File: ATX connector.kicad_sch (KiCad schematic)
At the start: 14 parts, among them J402 ATX-24, J403 ATX-20

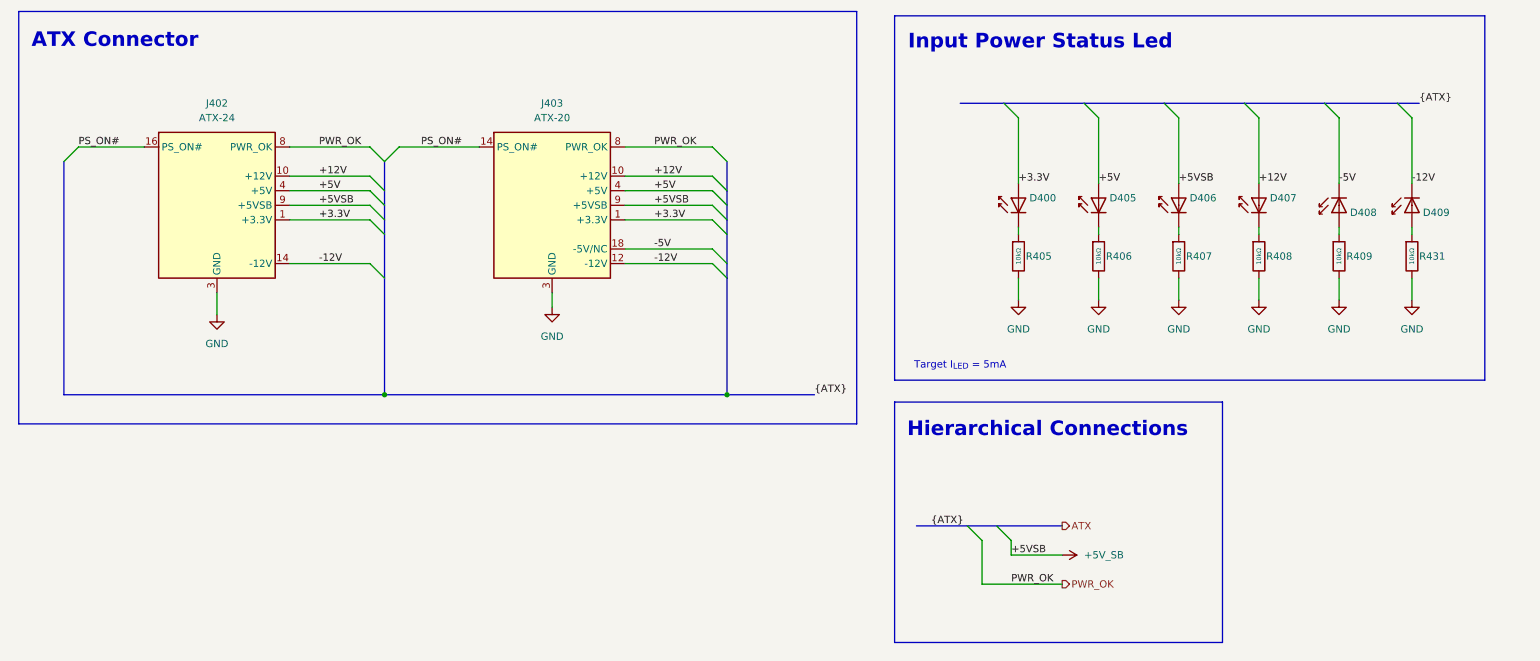
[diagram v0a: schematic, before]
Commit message: added 4 pin ATX connectors
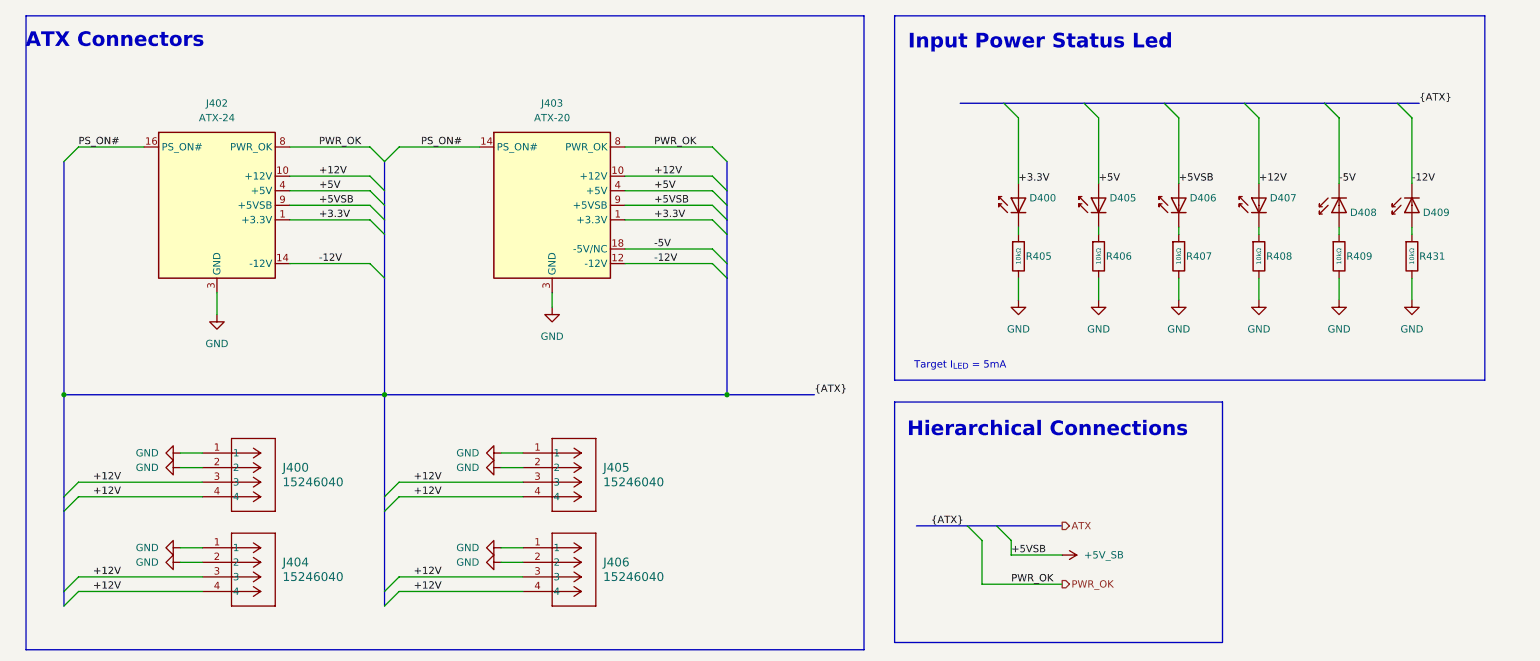
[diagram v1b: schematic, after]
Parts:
- added J400, J404, J405, J406: 15246040, footprints:CONN_SDA-42404_04_MOL, symbol 2025-11-30_18-16-43:15246040
- J403: footprint (none) -> Connector_Molex:Molex_Mini-Fit_Jr_5566-20A2_2x10_P4.20mm_Vertical
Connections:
- net +12V: now also J400.3, J400.4, J404.3, J404.4, J405.3, J405.4, J406.3, J406.4
- net GND: now also J400.1, J400.2, J404.1, J404.2, J405.1, J405.2, J406.1, J406.2
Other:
- note added: "ATX Connectors"
- note removed: "ATX Connector"

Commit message: removed 20pin ATX connector
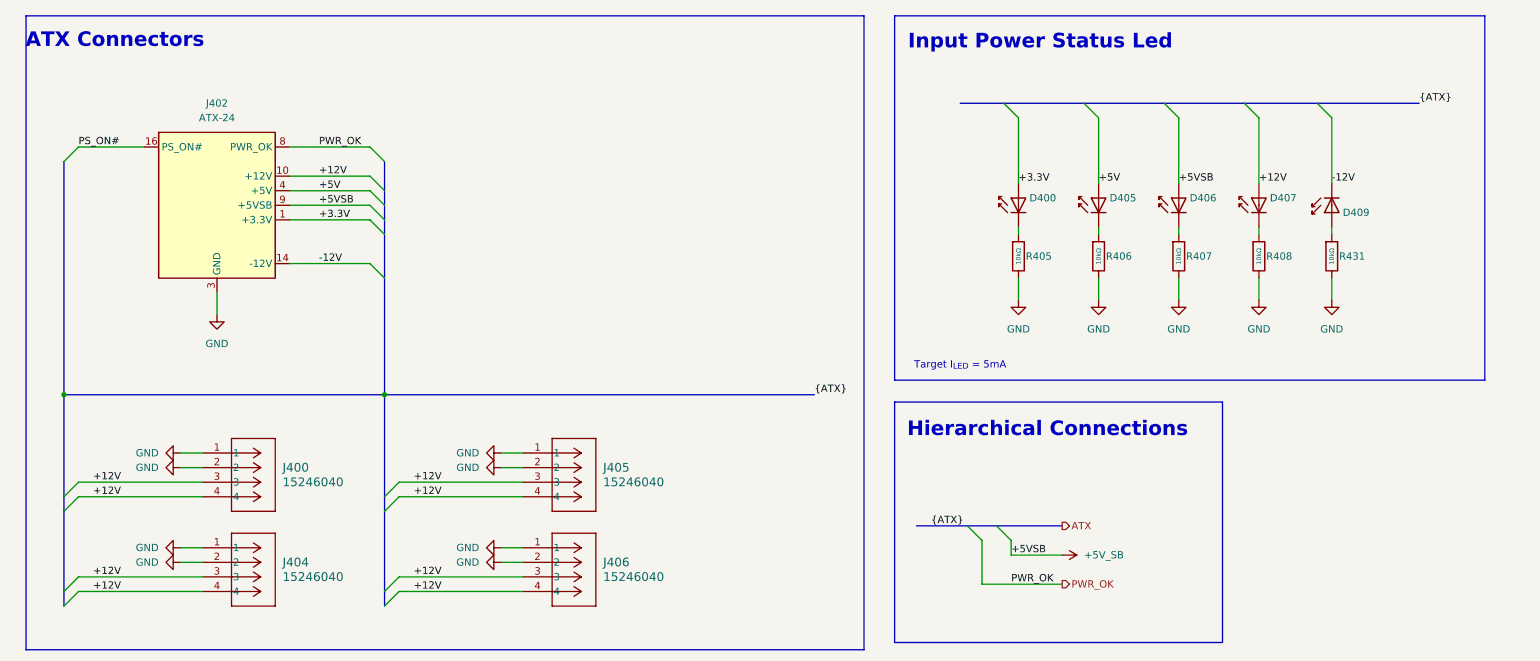
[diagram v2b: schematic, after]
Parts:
- removed D408: Green, PCM_JLCPCB:D_0603, symbol PCM_JLCPCB-Diodes:LED,0603,Green
- removed J403: ATX-20, Connector_Molex:Molex_Mini-Fit_Jr_5566-20A2_2x10_P4.20mm_Vertical, symbol Connector:ATX-20
- removed R409: 10kΩ, PCM_JLCPCB:R_0402, symbol PCM_JLCPCB-Resistors:0402,10kΩ
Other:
- moved on the sheet: D409, R431

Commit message: fixed PS_ON# switching
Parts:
- J402: footprint Connector_Molex:Molex_Mini-Fit_Jr_5566-24A2_2x12_P4.20mm_Vertical -> Connector_Molex:Molex_Mini-Fit_Jr_5569-24A2_2x12_P4.20mm_Horizontal
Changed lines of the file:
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@@
 			)
 		)
-		(property "Footprint" "Connector_Molex:Molex_Mini-Fit_Jr_5566-24A2_2x12_P4.20mm_Vertical"
+		(property "Footprint" "Connector_Molex:Molex_Mini-Fit_Jr_5569-24A2_2x12_P4.20mm_Horizontal"
 			(at 57.15 55.88 0)
 			(effects

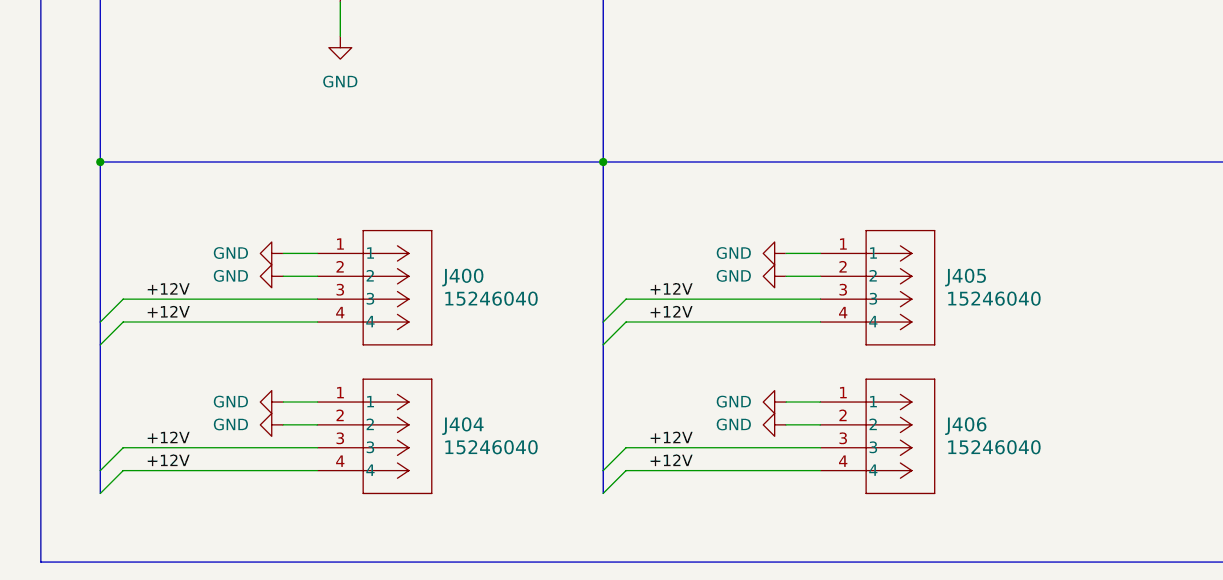
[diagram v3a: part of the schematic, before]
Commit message: removed III out of IV 4 pin connector
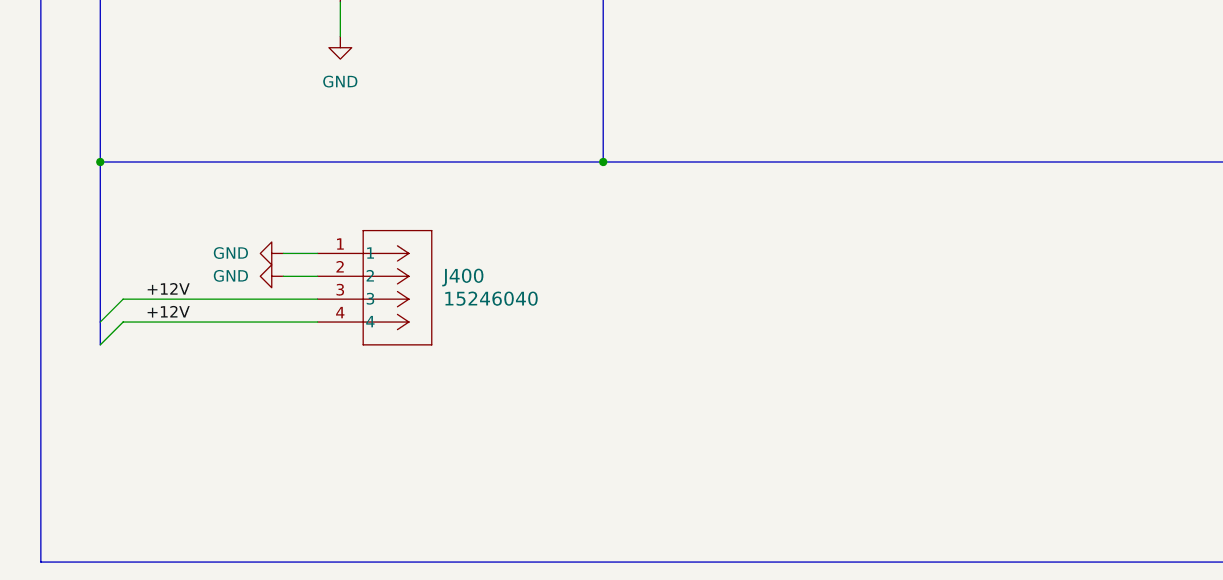
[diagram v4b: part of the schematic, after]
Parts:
- removed J404, J405, J406: 15246040, footprints:CONN_SDA-42404_04_MOL, symbol 2025-11-30_18-16-43:15246040

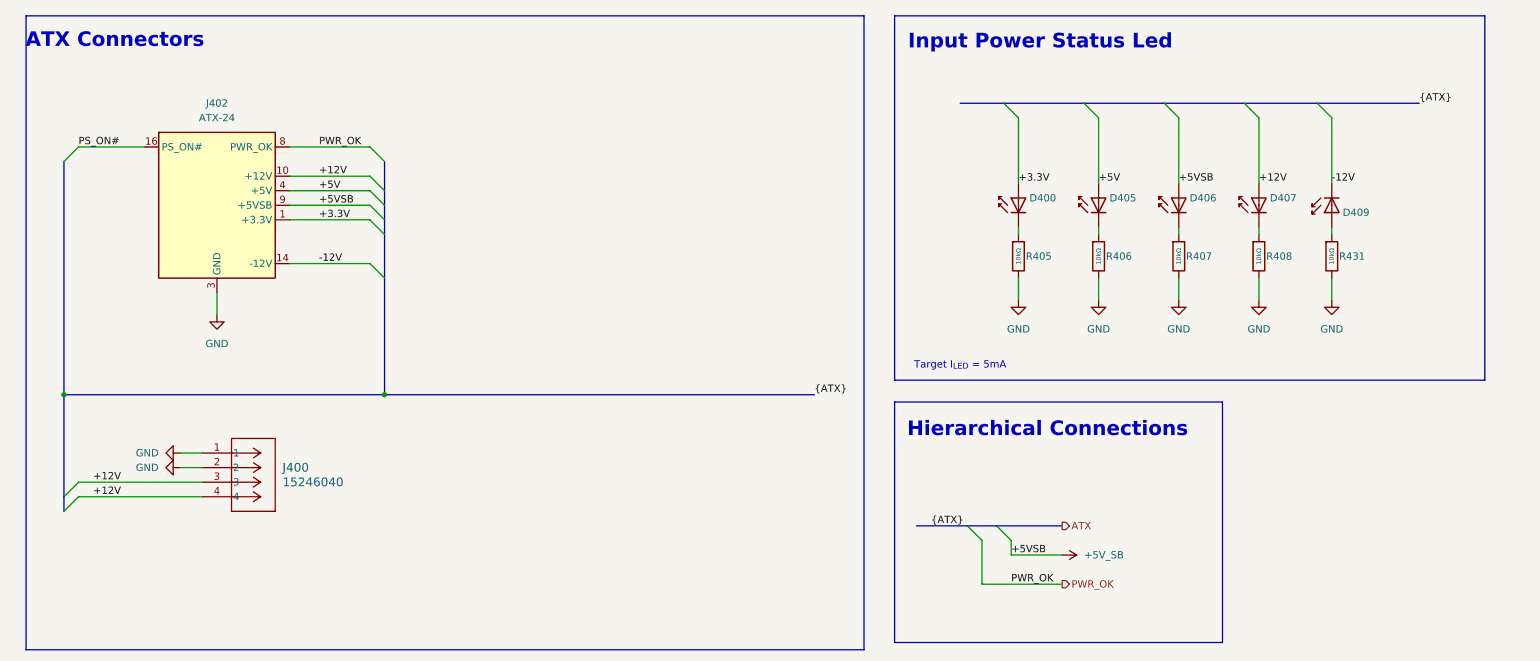
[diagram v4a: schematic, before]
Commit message: removed 3V3 converter
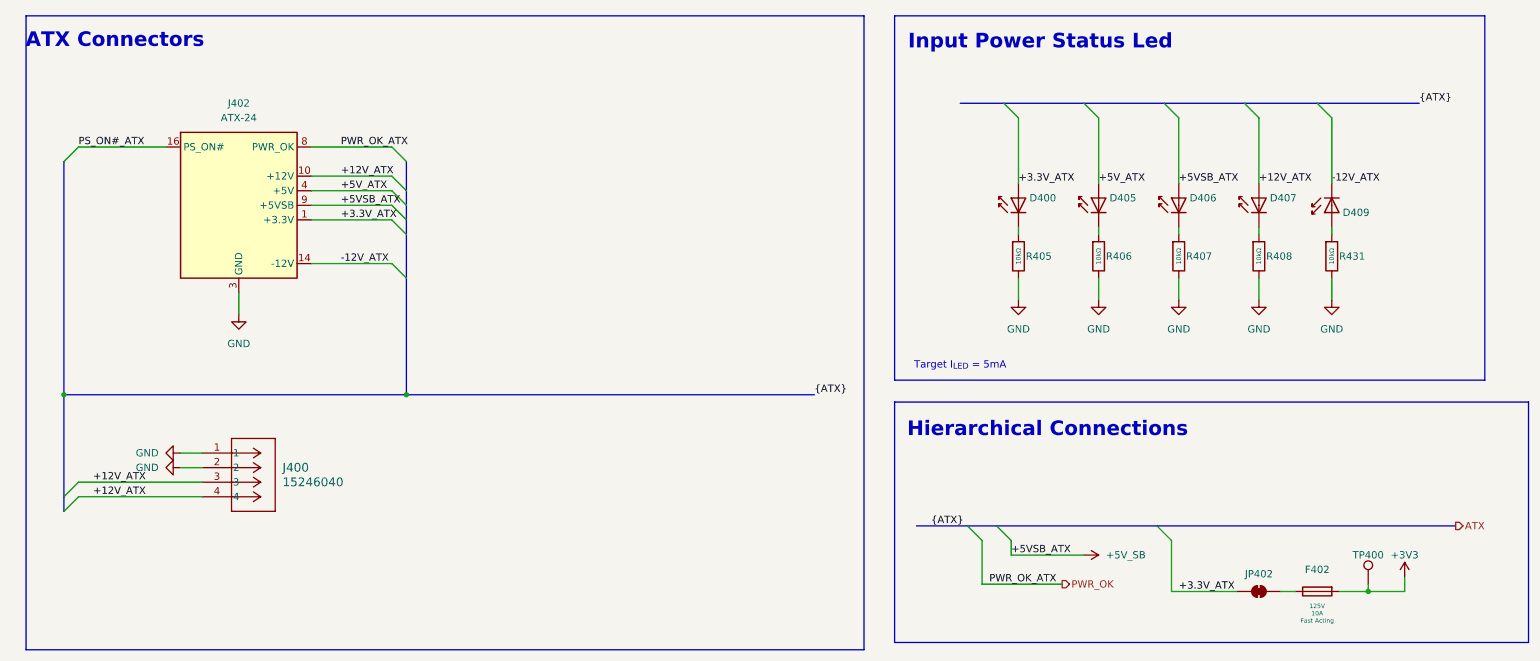
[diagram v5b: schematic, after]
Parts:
- added F402: 10A, FuseCustom:Fuse_2410_6125, symbol FuseCustom:JFC2410FS-2100FS
- added JP402: Test Buck Vout, Jumper:SolderJumper-2_P1.3mm_Open_TrianglePad1.0x1.5mm, symbol Jumper:SolderJumper_2_Bridged
- added TP400: TestPoint, TestPoint:TestPoint_Pad_D1.0mm, symbol Connector:TestPoint
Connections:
- net +12V renamed +12V_ATX
- net +3.3V renamed +3.3V_ATX
- net +3.3V_ATX: now also JP402.1 (A)
- net +5V renamed +5V_ATX
- net -12V renamed -12V_ATX
- net PS_ON# renamed PS_ON#_ATX
- new net: F402.2, JP402.2 (B)
- new net +3V3: F402.1, TP400.1
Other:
- moved on the sheet: J402

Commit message: routing progress
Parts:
- J402: footprint Connector_Molex:Molex_Mini-Fit_Jr_5569-24A2_2x12_P4.20mm_Horizontal -> Connector_Molex:Molex_Mini-Fit_Jr_5566-24A2_2x12_P4.20mm_Vertical
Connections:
- net 3V3_BF: now reaches F402.2, JP402.2 (B)
- net PWR_OK renamed PWR_OK_ATX
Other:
- moved on the sheet: F402, TP400
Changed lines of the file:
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@@
 	)
 	(junction
-		(at 257.81 120.65)
+		(at 269.24 120.65)
 		(diameter 0)
 		(color 0 0 0 0)
@@
 	(wire
 		(pts
-			(xy 252.73 120.65) (xy 257.81 120.65)
+			(xy 264.16 120.65) (xy 269.24 120.65)
 		)
 		(stroke
@@
 	(wire
 		(pts
-			(xy 33.02 43.18) (xy 48.26 43.18)
-		)
-		(stroke
-			(width 0)
-			(type default)
-		)
-	)
-	(wire
-		(pts
 			(xy 54.61 99.06) (xy 50.8 99.06)
 		)
@@
 	(wire
 		(pts
-			(xy 242.57 120.65) (xy 245.11 120.65)
+			(xy 242.57 120.65) (xy 256.54 120.65)
 		)
 		(stroke
@@
 	(wire
 		(pts
-			(xy 257.81 120.65) (xy 264.16 120.65)
+			(xy 269.24 120.65) (xy 275.59 120.65)
 		)
 		(stroke
@@
 	(wire
 		(pts
-			(xy 264.16 118.11) (xy 264.16 120.65)
+			(xy 275.59 118.11) (xy 275.59 120.65)
 		)
 		(stroke
@@
 	(wire
 		(pts
-			(xy 257.81 119.38) (xy 257.81 120.65)
+			(xy 269.24 119.38) (xy 269.24 120.65)
 		)
 		(stroke
@@
 	(wire
 		(pts
+			(xy 33.02 43.18) (xy 48.26 43.18)
+		)
+		(stroke
+			(width 0)
+			(type default)
+		)
+	)
+	(wire
+		(pts
 			(xy 251.46 38.1) (xy 251.46 49.53)
 		)
@@
 		)
 	)
-	(label "{ATX}"
-		(at 181.61 109.22 0)
-		(effects
-			(font
-				(size 1.27 1.27)
-			)
-			(justify left bottom)
-		)
-	)
 	(label "+5V_ATX"
 		(at 78.74 50.8 0)
@@
 	)
 	(label "+5VSB_ATX"
-		(at 78.74 53.34 0)
+		(at 77.47 53.34 0)
 		(effects
 			(font
@@
 		)
 	)
+	(label "{ATX}"
+		(at 181.61 109.22 0)
+		(effects
+			(font
+				(size 1.27 1.27)
+			)
+			(justify left bottom)
+		)
+	)
 	(label "+12V_ATX"
 		(at 35.56 104.14 0)
@@
 	)
 	(label "PS_ON#_ATX"
-		(at 33.02 43.18 0)
+		(at 34.29 43.18 0)
+		(effects
+			(font
+				(size 1.27 1.27)
+			)
+			(justify left bottom)
+		)
+	)
+	(label "3V3_BF"
+		(at 246.38 120.65 0)
 		(effects
 			(font
@@
 		)
 	)
-	(hierarchical_label "PWR_OK"
+	(hierarchical_label "PWR_OK_ATX"
 		(shape output)
 		(at 204.47 119.38 0)
@@
 		)
 	)
-	(hierarchical_label "ATX"
+	(hierarchical_label "ATX{ATX}"
 		(shape output)
 		(at 273.05 109.22 0)
@@
 	(symbol
 		(lib_id "Connector:TestPoint")
-		(at 257.81 119.38 0)
+		(at 269.24 119.38 0)
 		(unit 1)
 		(exclude_from_sim no)
@@
 		(dnp no)
 		(property "Reference" "TP400"
-			(at 257.81 114.3 0)
+			(at 269.24 114.3 0)
 			(effects
 				(font
@@
 		)
 		(property "Value" "TestPoint"
-			(at 260.35 117.348 0)
+			(at 271.78 117.348 0)
 			(effects
 				(font
@@
 		)
 		(property "Footprint" "TestPoint:TestPoint_Pad_D1.0mm"
-			(at 262.89 119.38 0)
+			(at 274.32 119.38 0)
 			(effects
 				(font
@@
 		)
 		(property "Datasheet" "~"
-			(at 262.89 119.38 0)
+			(at 274.32 119.38 0)
 			(effects
 				(font
@@
 		)
 		(property "Description" "test point"
-			(at 257.81 119.38 0)
+			(at 269.24 119.38 0)
 			(effects
 				(font
@@
 	(symbol
 		(lib_id "FuseCustom:JFC2410FS-2100FS")
-		(at 248.92 120.65 270)
+		(at 260.35 120.65 270)
 		(unit 1)
 		(exclude_from_sim no)
@@
 		(dnp no)
 		(property "Reference" "F402"
-			(at 248.92 116.84 90)
+			(at 260.35 116.84 90)
 			(effects
 				(font
@@
 		)
 		(property "Value" "10A"
-			(at 243.84 120.65 0)
+			(at 255.27 120.65 0)
 			(effects
 				(font
@@
 		)
 		(property "Footprint" "FuseCustom:Fuse_2410_6125"
-			(at 244.348 120.65 0)
+			(at 255.778 120.65 0)
 			(effects
 				(font
@@
 		)
 		(property "Datasheet" "https://jlcpcb.com/api/file/downloadByFileSystemAccessId/8588899540782604288"
-			(at 244.094 120.65 0)
+			(at 255.524 120.65 0)
 			(effects
 				(font
@@
 		)
 		(property "Description" "-55℃~+125℃ 10A 125V 125V 50A Surface Mount Fuse 2410 Disposable fuses ROHS"
-			(at 244.094 120.65 0)
+			(at 255.524 120.65 0)
 			(effects
 				(font
@@
 		)
 		(property "Manufacturer" "Shenzhen JDT Fuse"
-			(at 244.348 120.65 0)
+			(at 255.778 120.65 0)
 			(effects
 				(font
@@
 		)
 		(property "Name" "JFC2410FS-2100FS"
-			(at 244.348 120.65 0)
+			(at 255.778 120.65 0)
 			(effects
 				(font
@@
 		)
 		(property "Package" "2410"
-			(at 244.348 120.904 0)
+			(at 255.778 120.904 0)
 			(effects
 				(font
@@
 		)
 		(property "Current Trigger" "10A"
-			(at 248.92 124.46 90)
+			(at 260.35 124.46 90)
 			(do_not_autoplace yes)
 			(effects
@@
 		)
 		(property "Voltage Rating" "125V"
-			(at 248.92 123.19 90)
+			(at 260.35 123.19 90)
 			(do_not_autoplace yes)
 			(effects
@@
 		)
 		(property "Time Sensitivity" "Fast Acting"
-			(at 248.92 125.73 90)
+			(at 260.35 125.73 90)
 			(do_not_autoplace yes)
 			(effects
@@
 		)
 		(property "Assembly Type" "SMT Assembly"
-			(at 244.094 120.396 0)
+			(at 255.524 120.396 0)
 			(effects
 				(font
@@
 		)
 		(property "LCSC" "C136374"
-			(at 244.348 120.65 0)
+			(at 255.778 120.65 0)
 			(effects
 				(font
@@
 	(symbol
 		(lib_id "power:+5V")
-		(at 264.16 118.11 0)
+		(at 275.59 118.11 0)
 		(unit 1)
 		(exclude_from_sim no)
@@
 		(dnp no)
 		(property "Reference" "#PWR0411"
-			(at 264.16 121.92 0)
+			(at 275.59 121.92 0)
 			(effects
 				(font
@@
 		)
 		(property "Value" "+3V3"
-			(at 264.16 114.3 0)
+			(at 275.59 114.3 0)
 			(effects
 				(font
@@
 		)
 		(property "Footprint" ""
-			(at 264.16 118.11 0)
+			(at 275.59 118.11 0)
 			(effects
 				(font
@@
 		)
 		(property "Datasheet" ""
-			(at 264.16 118.11 0)
+			(at 275.59 118.11 0)
 			(effects
 				(font
@@
 		)
 		(property "Description" "Power symbol creates a global label with name \"+5V\""
-			(at 264.16 118.11 0)
+			(at 275.59 118.11 0)
 			(effects
 				(font
@@
 			)
 		)
-		(property "Footprint" "Connector_Molex:Molex_Mini-Fit_Jr_5569-24A2_2x12_P4.20mm_Horizontal"
+		(property "Footprint" "Connector_Molex:Molex_Mini-Fit_Jr_5566-24A2_2x12_P4.20mm_Vertical"
 			(at 60.96 55.88 0)
 			(effects

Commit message: finished routing
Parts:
- JP402: footprint Jumper:SolderJumper-2_P1.3mm_Open_TrianglePad1.0x1.5mm -> Jumper:SolderJumper-2_P1.3mm_Bridged_RoundedPad1.0x1.5mm
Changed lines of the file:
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@@
 			)
 		)
-		(property "Footprint" "Jumper:SolderJumper-2_P1.3mm_Open_TrianglePad1.0x1.5mm"
+		(property "Footprint" "Jumper:SolderJumper-2_P1.3mm_Bridged_RoundedPad1.0x1.5mm"
 			(at 238.76 120.65 0)
 			(effects
